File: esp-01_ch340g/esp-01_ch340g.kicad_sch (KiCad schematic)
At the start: 7 parts, among them SW1 Flash, SW2 Reset, SW3 Flash2, SW4 Reset2, U1 ESP-01

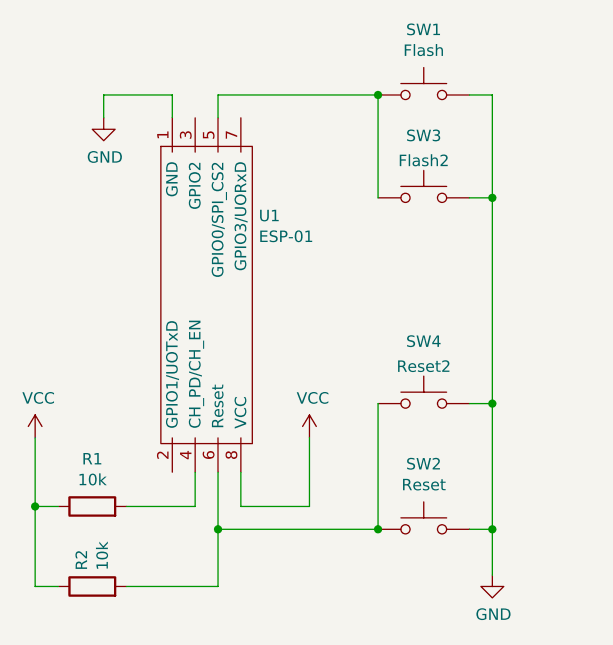
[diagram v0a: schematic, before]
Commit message: esp-01 programmer board
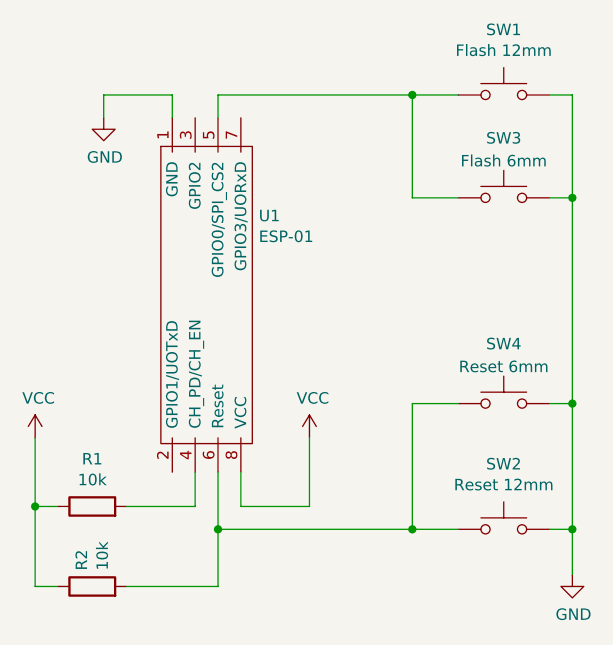
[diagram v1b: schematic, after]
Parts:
- SW1: value Flash -> Flash 12mm
- SW2: value Reset -> Reset 12mm
- SW3: value Flash2 -> Flash 6mm
- SW4: value Reset2 -> Reset 6mm
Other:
- moved on the sheet: SW1, SW2, SW3, SW4
